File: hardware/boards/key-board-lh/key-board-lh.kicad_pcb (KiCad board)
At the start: 2 copper layers, 84 x 42 mm, 33 parts

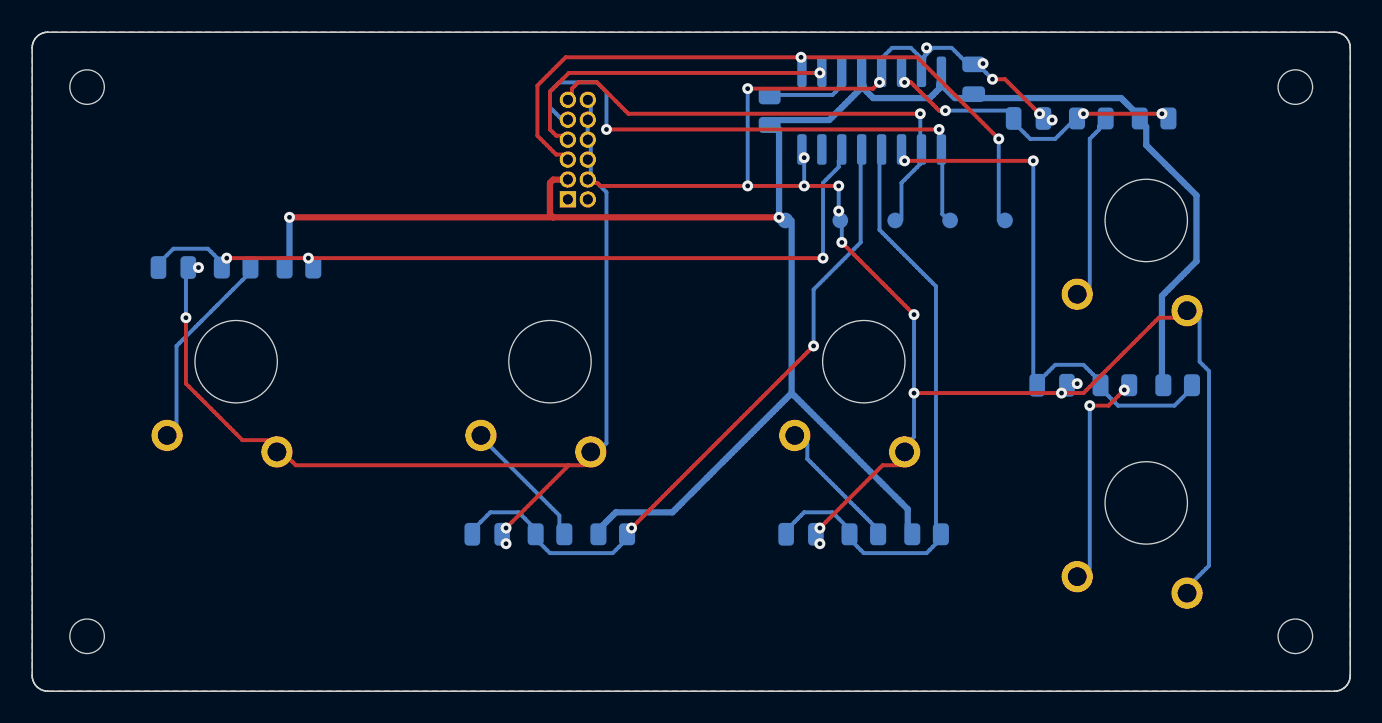
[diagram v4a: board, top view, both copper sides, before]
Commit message: WIP: layout-side fixes (networks as T, via-in-pad, segment merge, silk, stackup, TP-SER, drills)
Co-Authored-By: Claude Opus 5.5 <noreply@anthropic.com>
Claude-Session: https://claude.ai/code/session_01LmB4muFXnoLprWX4JzuJ5A
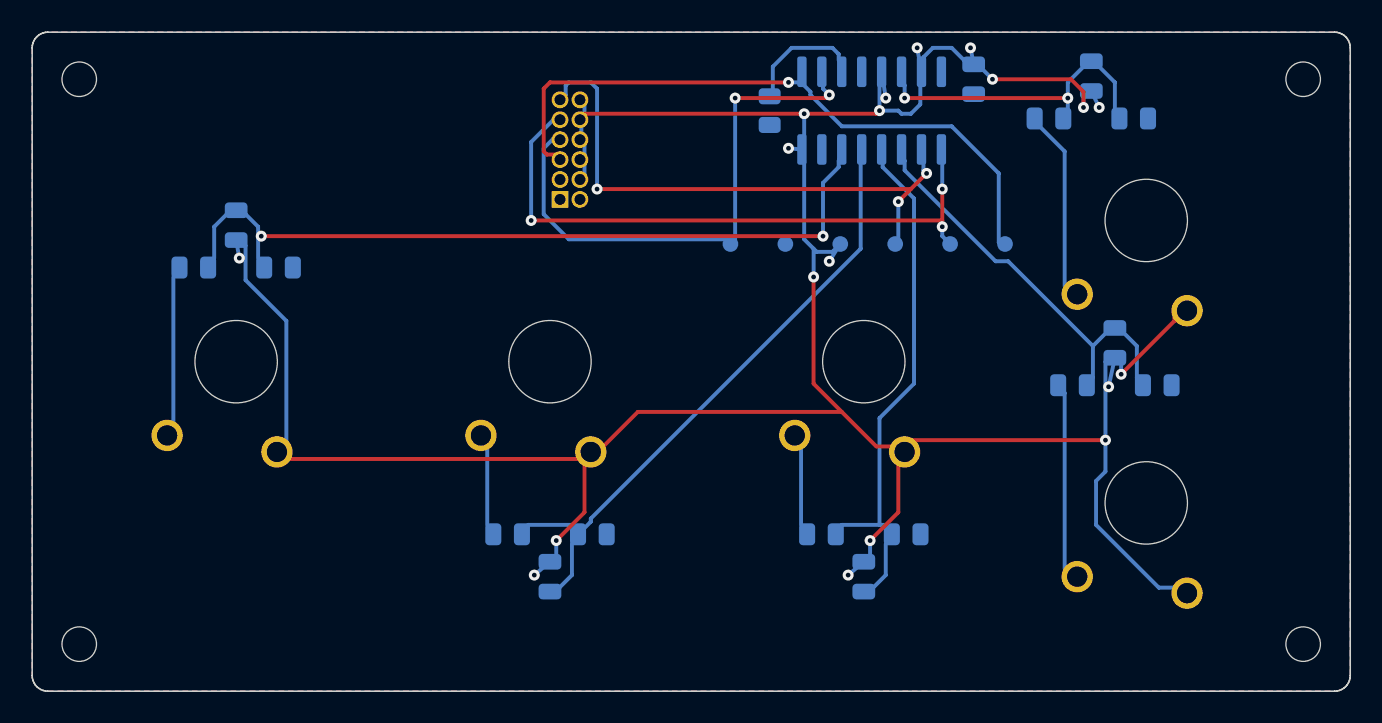
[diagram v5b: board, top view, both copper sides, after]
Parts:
- added TP-SER-LH: test pad, TestPoint:TestPoint_Pad_D1.0mm, B.Cu at (141.5, 114.0)
- moved C-KEY-LH1 4.83 mm to (110.0, 112.8), turned to -90 degrees
- moved C-KEY-LH4 4.83 mm to (166.0, 120.3), turned to -90 degrees
- moved C-KEY-LH5 4.83 mm to (164.5, 103.3), turned to -90 degrees
- moved C-KEY-LH2 4.83 mm to (130.0, 135.2), turned to 90 degrees
- moved C-KEY-LH3 4.83 mm to (150.0, 135.2), turned to 90 degrees
- moved R-KEY-SER-LH1 2.70 mm to (107.3, 115.5), turned to 180 degrees
- moved R-KEY-SER-LH2 2.70 mm to (127.3, 132.5), turned to 180 degrees
- moved R-KEY-SER-LH3 2.70 mm to (147.3, 132.5), turned to 180 degrees
- moved R-KEY-SER-LH4 2.70 mm to (163.3, 123.0), turned to 180 degrees
- moved R-KEY-SER-LH5 2.70 mm to (161.8, 106.0), turned to 180 degrees
- moved TP-3V3-LH 1.50 mm to (145.0, 114.0)
- moved TP-GND-LH 1.50 mm to (148.5, 114.0)
- moved TP-QH-LH 1.50 mm to (159.0, 114.0)
- moved TP-SCK-LH 1.50 mm to (152.0, 114.0)
- moved TP-SHLD-LH 1.50 mm to (155.5, 114.0)
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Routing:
- net V3V3_CHAIN_LH: track 129.1 -> 0.00 mm, vias 2 -> 0
- net /CHAIN_SER_LH: track 21.5 -> 34.5 mm, vias 1 -> 2
- net /KEY_LH4: track 33.8 -> 25.5 mm, vias 2 -> 0
- net GND_CHAIN: track 179.6 -> 186.1 mm, vias 23 -> 19
- net /CHAIN_SCK: track 30.4 -> 35.9 mm, vias 1 -> 3
- net /CHAIN_SHLD: track 34.6 -> 39.1 mm, vias 2 -> 3
- net /KEY_LH3: track 36.6 -> 33.0 mm
- net /KEY_LH2: track 41.3 -> 38.7 mm, vias 2 -> 0
- net /KEY_FREE3: track 4.77 -> 7.21 mm
- net /HOP_LH_LT: track 43.9 -> 41.5 mm, vias 2 -> 1
- net /LH2/SWITCH_LEG: track 7.74 -> 5.81 mm
- net /LH1/SWITCH_LEG: track 12.1 -> 10.2 mm
- net /LH3/SWITCH_LEG: track 7.62 -> 5.81 mm
- net /LH4/SWITCH_LEG: track 13.4 -> 11.8 mm, vias 2 -> 0
- net /KEY_LH5: track 18.2 -> 19.7 mm, vias 4 -> 2
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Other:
- board text added: "SER"

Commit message: LH key board re-laid out: networks as T's, no via in any pad, merged tracks
Layout side of the 2026-09-27 wave (closed by id in its VERIFIED.md):
- Each key network is a T round its KEY node (layout.yaml networks:,
  tools/pcb.py network_parts), so no pad of another net stands between
  the node's three pads (K3-7).
- The router keeps every via off every SMD pad, its own net's too (K3-1),
  merges collinear runs on grid cells rather than rounded mm (K3-6: 684
  segments to about 240, no collinear joint left), routes the power rail
  first, and gives a net that failed a rip-up of the nets across its pads.
- The library silkscreen is widened to the board house's line and dropped
  where it comes nearer a pad than its limit; labels are searched clear of
  each other; the register's label is beside it; J-CHAIN gets a mouth
  arrow and a pin-1 dot clear of the pad (K3-3, K3-13, K2-7).
- The PCB carries its title block and a full stackup: finish, mask and
  silk colour, 1 oz copper (K3-9).
- J-CHAIN drills 0.70 on 1.07 pads, KS-33 pins 1.3 (K3-4, K3-5).
- A sixth test pad on SER, on both boards (K1-11); the free-bit pull-up,
  C-KEY and R-KEY-SER notes and the register's pin source corrected on
  the sheets (K1-6, K1-9, K1-14).
- The dead ribbon-strip code is gone (K7-9).

pcb.py check: 0 errors under the stricter checks; kicad.py check PASS.

Co-Authored-By: Claude Opus 5.5 <noreply@anthropic.com>
Claude-Session: https://claude.ai/code/session_01LmB4muFXnoLprWX4JzuJ5A
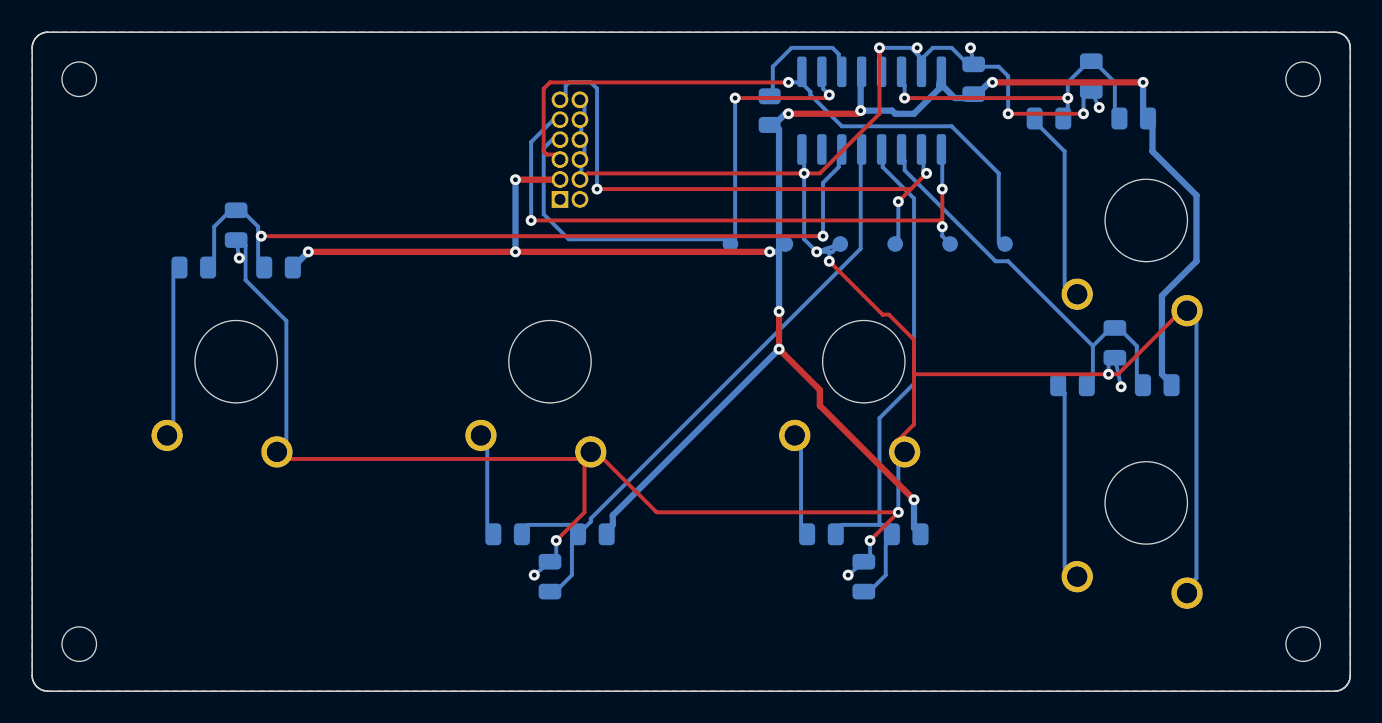
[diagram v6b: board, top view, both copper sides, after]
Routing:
- net V3V3_CHAIN_LH: track 0.00 -> 133.8 mm, vias 0 -> 11
- net GND_CHAIN: track 186.1 -> 190.7 mm, vias 19 -> 17

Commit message: Key boards: a do-not-fit bulk capacitor footprint; decoupler across the register's supply pins
- C-BULK-CHAIN-LH/-RH: a 10uF 0805 footprint on each key board's 3V3,
  dnp and out of every order, fitted at bring-up only if the FB-CHAIN /
  C-DECOUPLE-165 LC rings (K1-13). New row C-BULK-CHAIN beside FB-CHAIN.
- pcb.py carries the symbol's "Do not populate" and "Exclude from BOM"
  to the footprint, so a dnp part passes schematic parity.
- C-DECOUPLE-165-LH lies across the ends of U-KEYS pins 16 and 15, each a
  2.25 mm stub (K3-8's loop closed through the plane 12.9 mm away), and
  ground now routes to every pin without leaning on the pour.

Co-Authored-By: Claude Opus 5.5 <noreply@anthropic.com>
Claude-Session: https://claude.ai/code/session_01LmB4muFXnoLprWX4JzuJ5A
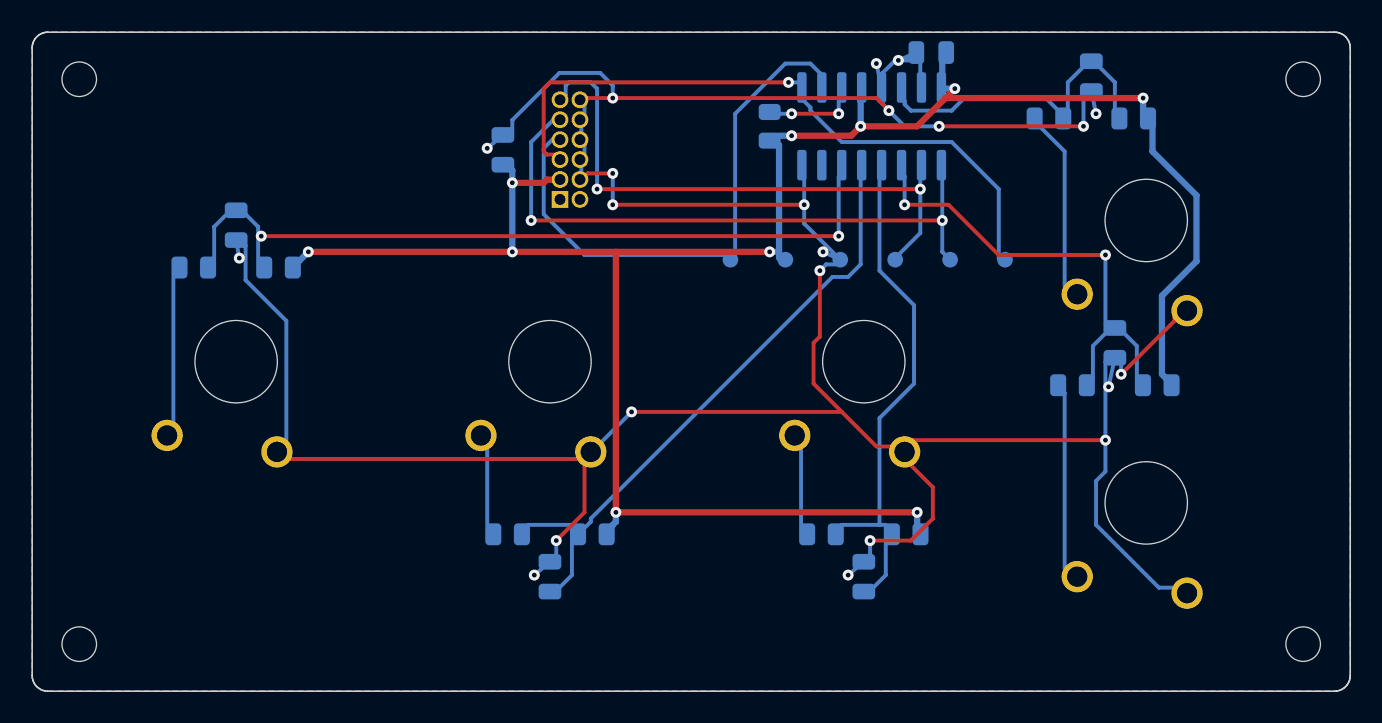
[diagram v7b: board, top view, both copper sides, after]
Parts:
- added C-BULK-CHAIN-LH: 10uF DNP, Capacitor_SMD:C_0805_2012Metric, B.Cu at (127.0, 108.0)
- moved C-DECOUPLE-165-LH 3.19 mm to (154.3, 101.8), turned to 180 degrees
- moved R-KEY-PU-FREE3 1.00 mm to (144.0, 106.5)
- moved TP-3V3-LH 1.00 mm to (145.0, 115.0)
- moved TP-GND-LH 1.00 mm to (148.5, 115.0)
- moved TP-QH-LH 1.00 mm to (159.0, 115.0)
- moved TP-SCK-LH 1.00 mm to (152.0, 115.0)
- moved TP-SER-LH 1.00 mm to (141.5, 115.0)
- moved TP-SHLD-LH 1.00 mm to (155.5, 115.0)
- moved U-KEYS-LH 1.00 mm to (150.5, 106.5)
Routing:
- net GND_CHAIN: track 190.7 -> 212.8 mm, vias 17 -> 22
- net V3V3_CHAIN_LH: track 133.8 -> 137.3 mm, vias 11 -> 10
- net /KEY_LH4: track 25.5 -> 28.6 mm, vias 0 -> 2
- net /KEY_FREE3: track 7.21 -> 5.21 mm, vias 0 -> 2
- net /KEY_LH3: track 33.0 -> 32.1 mm
- net /CHAIN_SER_LH: track 34.5 -> 35.1 mm, vias 2 -> 0
- net /KEY_LH5: track 19.7 -> 19.3 mm, vias 2 -> 0
- net /CHAIN_SCK: track 35.9 -> 36.3 mm, vias 3 -> 2
- net /CHAIN_SHLD: vias 3 -> 2

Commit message: Register becomes the SN74HCS165; key-board standoff gets its washer
The owner's two decisions after the LH wave:

SN74HCS165 (TI, Schmitt-trigger inputs, no input transition-rate limit):
- key-register.kicad_sch U-KEYS: value, Manufacturer, MPN SN74HCS165DR,
  LCSC C2864745, Pins_source (TI p.3), Note; same SOIC-16 and symbol.
- U-KEYS row: what the part must be, and that a substitute needs Schmitt
  inputs with no rate limit (not a 74HC165, not a 74LV165A).
- key-release-time 119.9 -> 138.7 us and key-press-time 5.92 -> 9.87 us,
  against TI's thresholds at their guaranteed extremes (no 3.3 V row: the
  table's largest VT+ and smallest VT- ratios). Old spellings grepped first
  and moved into forbidden; the four patterns that matched the new value
  removed. The release is now just over half a scan, which changes no
  conclusion; the 10k trade recomputed (647 us).
- key-switch-network.md derives both against the HCS165; the retired HC165
  derivation moved to notes.md. ADR 0001 amended and its table cites the
  figures.

The standoff and washer:
- MSO4-M2-3 chosen, with an ISO 7092 / DIN 433 M2 washer under the board.
  Head flush in the plate, so the key boards' depth is standoff length +
  washer: switch.pcb_below_seat 3.4 -> 3.3, checked by a new rule, with the
  worst-case tolerance stack printed as a NOTE.
- The thumb switches keep their own depth, switch.thumb_pcb_below_seat:
  sharing the parameter moved them into the LED strip (clash.txt caught it).
- MECH-KB-WASHER row; MECH-KB-STANDOFF names the part and its US sources;
  MECH-KB-SCREW M2 x 4. The PCB's copper keep-out covers the washer.
- LH board re-laid out, checked (0 errors) and rendered.

Co-Authored-By: Claude Opus 5.5 <noreply@anthropic.com>
Claude-Session: https://claude.ai/code/session_01LmB4muFXnoLprWX4JzuJ5A
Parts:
- U-KEYS-LH: value 74HC165 -> 74HCS165
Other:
- board text added: "74HCS165"
- board text removed: "74HC165"
